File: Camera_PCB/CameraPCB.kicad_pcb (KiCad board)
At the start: 6 copper layers, 65.6 x 55 mm, 173 parts, among them J1 MIPI-CSI2, J2 USB_A, J3 SDA, J4 UART_0, J5 UART_2, J6 USB_C_Receptacle_PowerOnly_6P, SW1 PWR, SW2 RST, U1 AXP203, U2 V3s-eLQFP128, U3 TPS63020, U4 TPS63020, Y2 32.768kHz XTAL, Y4 24MHz XTAL

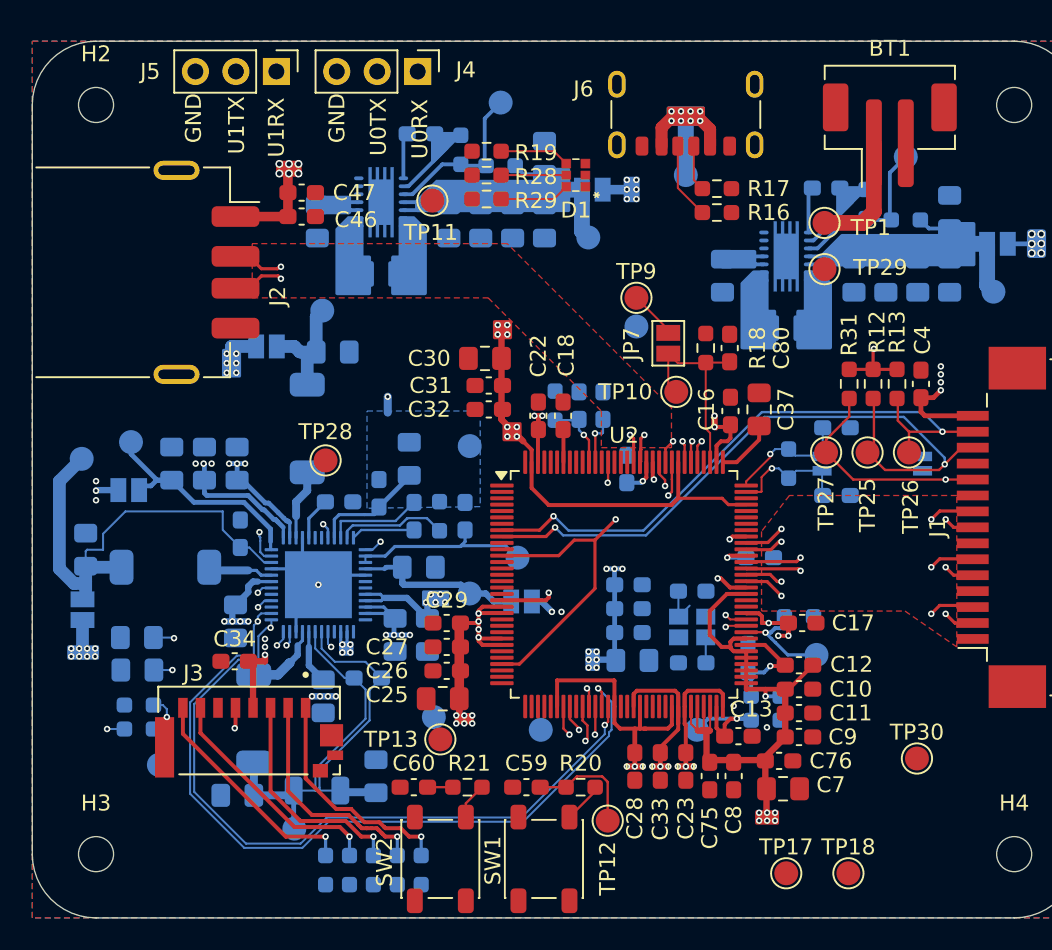
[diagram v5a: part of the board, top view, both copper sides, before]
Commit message: Only unconnected grounds in schematic. Still need to thoroughly clean up.
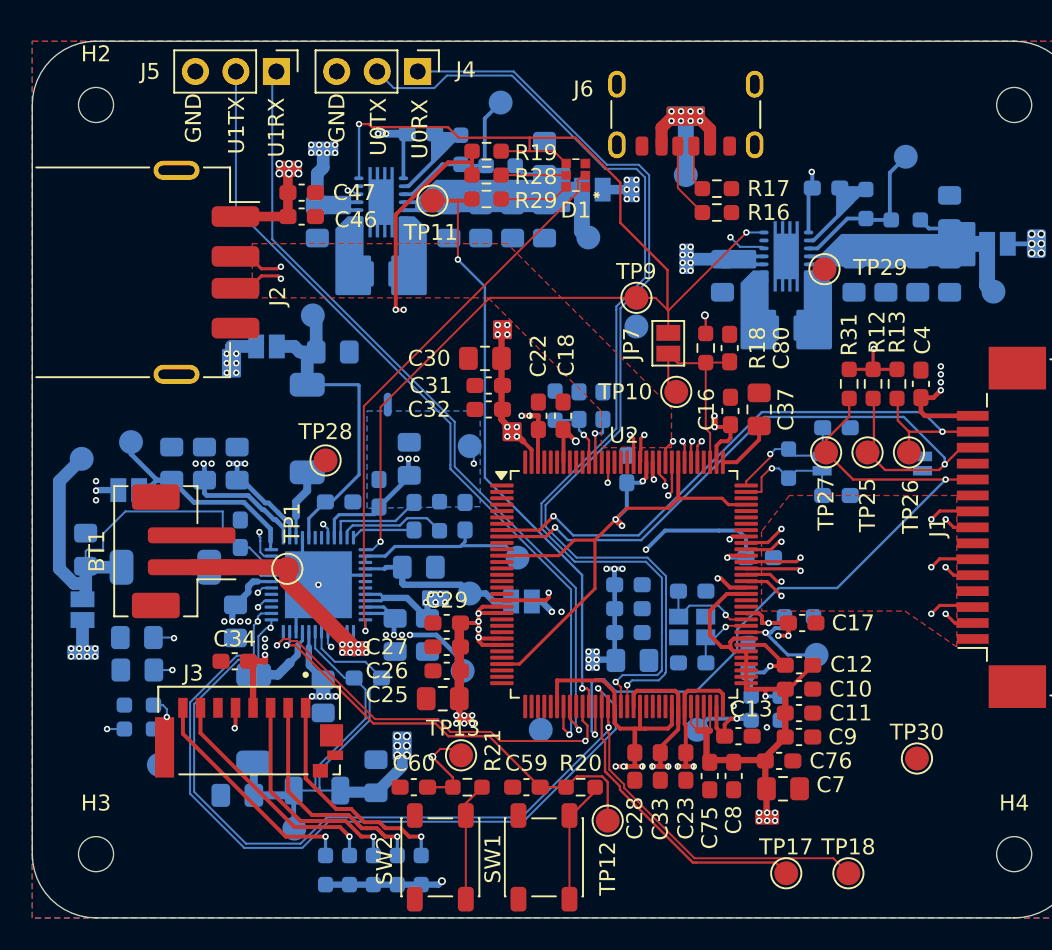
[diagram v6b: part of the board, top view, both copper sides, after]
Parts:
- moved BT1 51.4 mm to (124.5, 96.0), turned to 90 degrees
- moved TP1 40.1 mm to (131.0, 97.1), turned to 90 degrees
- moved TP2 3.42 mm to (142.0, 103.5)
- moved TP13 1.64 mm to (141.9, 108.8)
- moved TP4 0.66 mm to (132.6, 81.2)
- moved SW1 0.10 mm to (147.1, 115.2)
- moved SW2 0.10 mm to (140.6, 115.2)
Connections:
- D1 pad 4: Net-(D1-BA) -> PGOOD
- R19 pad 1: PGOOD -> HPVCC
- R19 pad 2: Net-(D1-BA) -> PGOOD
- R28 pad 1: VIPS -> HPVCC
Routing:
- net VIPS: track 37.4 -> 165.4 mm, vias 16 -> 22
- net VBAT: track 34.2 -> 136.6 mm, vias 4 -> 30
- net PGOOD: track 4.19 -> 76.0 mm, vias 1 -> 3
- net PWREN: track 0.97 -> 69.2 mm, vias 1 -> 4
- net UART0_TX: track 0.00 -> 64.4 mm, vias 0 -> 1
- net UART0_RX: track 0.00 -> 61.0 mm, vias 0 -> 1
- net HPVCC: track 227.5 -> 282.6 mm, vias 31 -> 36
- net UART2_TX: track 1.92 -> 52.3 mm
- net UART2_RX: track 1.71 -> 51.1 mm
- net STATUS_LED: track 1.19 -> 37.8 mm, vias 1 -> 2
- net CHGLED: track 0.00 -> 35.2 mm, vias 0 -> 1
- net CAM_EN0: track 15.8 -> 48.0 mm
- net IRQ: track 3.36 -> 25.5 mm
- net Net-(U1-N_OE): track 2.60 -> 24.2 mm, vias 1 -> 2
- net TWI0_SDA: track 45.5 -> 66.0 mm
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
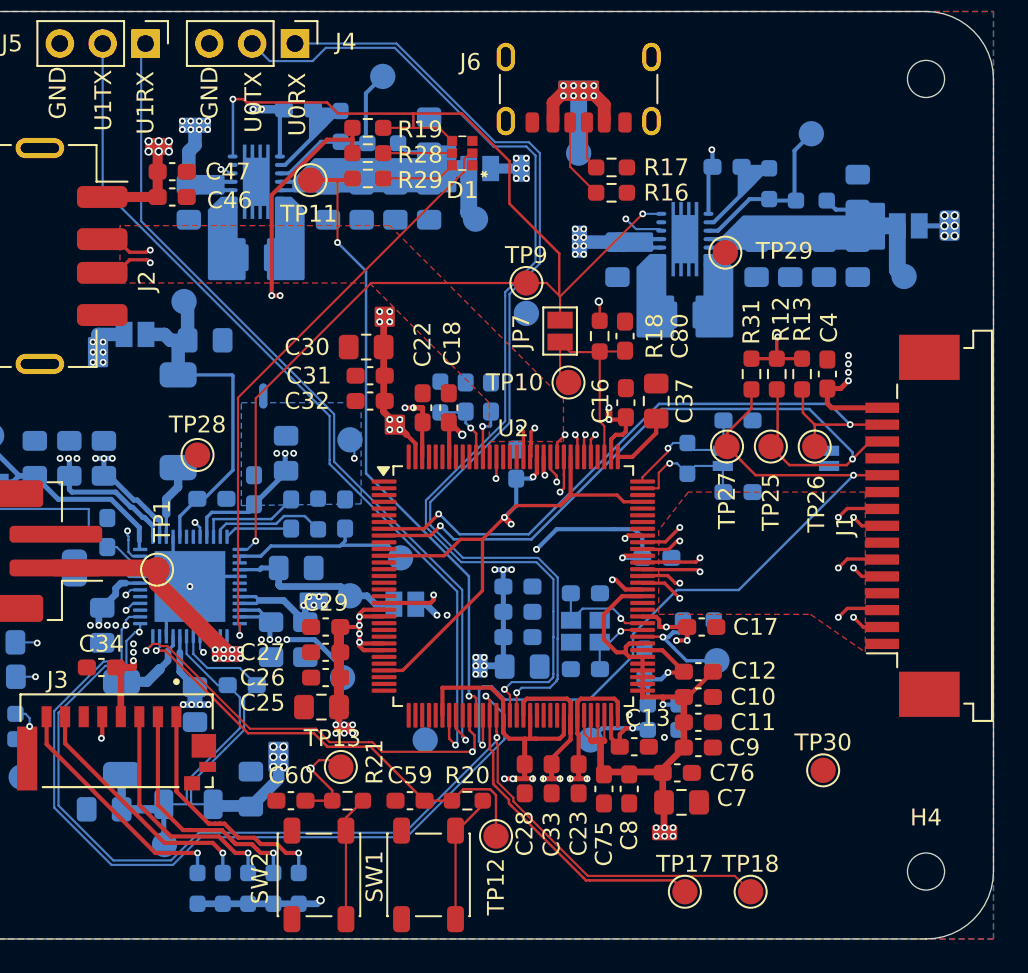
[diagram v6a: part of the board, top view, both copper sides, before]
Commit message: replaced all power traces with zones
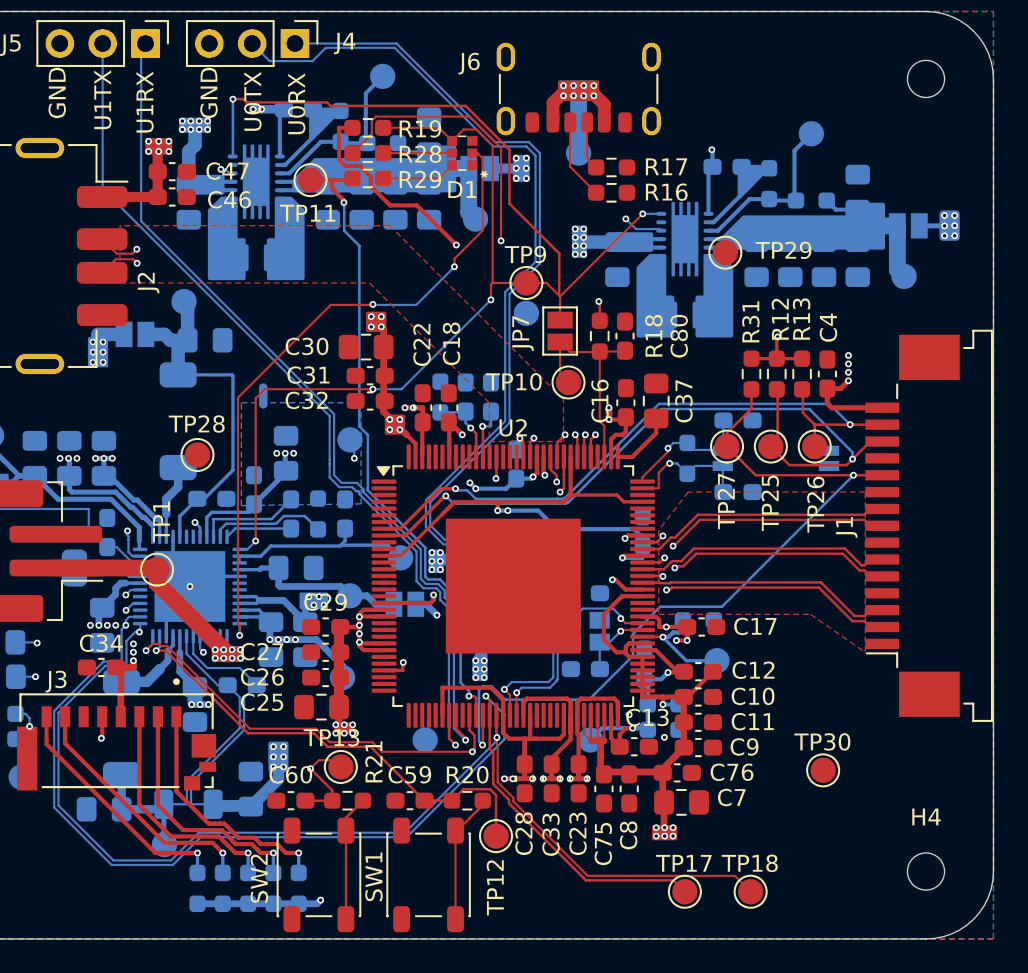
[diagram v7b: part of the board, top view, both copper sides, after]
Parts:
- moved C19 2.06 mm to (151.3, 101.2)
- moved C20 2.06 mm to (151.1, 98.0)
- moved C21 2.06 mm to (151.1, 99.5)
- moved C24 2.06 mm to (151.1, 96.5)
- moved C15 1.81 mm to (159.8, 94.8), turned to -90 degrees
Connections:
- R28 pad 1: HPVCC -> VBUS
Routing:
- net HPVCC: track 282.6 -> 106.3 mm, vias 36 -> 37
- net VIPS: track 165.4 -> 44.6 mm, vias 22 -> 21
- net VDD-CPU: track 167.5 -> 65.5 mm, vias 38 -> 41
- net VBAT: track 136.6 -> 49.1 mm
- net AVCC: track 82.1 -> 7.31 mm
- net VCC-DRAM: track 112.4 -> 41.4 mm
- net +5V: track 59.4 -> 7.92 mm
- net VCC-RTC: track 41.8 -> 7.53 mm, vias 5 -> 4
- net VBUS: track 51.4 -> 31.6 mm
- net PGOOD: track 76.0 -> 87.3 mm, vias 3 -> 5
- net CHGLED: track 35.2 -> 38.9 mm, vias 1 -> 3
- net USB_P: track 32.1 -> 33.3 mm
- net SDC0_D1: track 50.1 -> 51.4 mm
- net SDC0_CLK: track 47.4 -> 48.7 mm
- net UART2_RX: track 51.1 -> 52.0 mm
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- added copper zone on In2.Cu, net +5V
- added copper zone on In3.Cu, net AVCC
- added copper zone on In3.Cu, net HPVCC
- added copper zone on In2.Cu, net VBAT
- added copper zone on In3.Cu, net VBAT
- added copper zone on In3.Cu, net VBUS
- added copper zone on In2.Cu, net VCC-DRAM
- added copper zone on In3.Cu, net VCC-RTC
- added copper zone on In2.Cu, net VDD-CPU
- added copper zone on In2.Cu, net VIPS

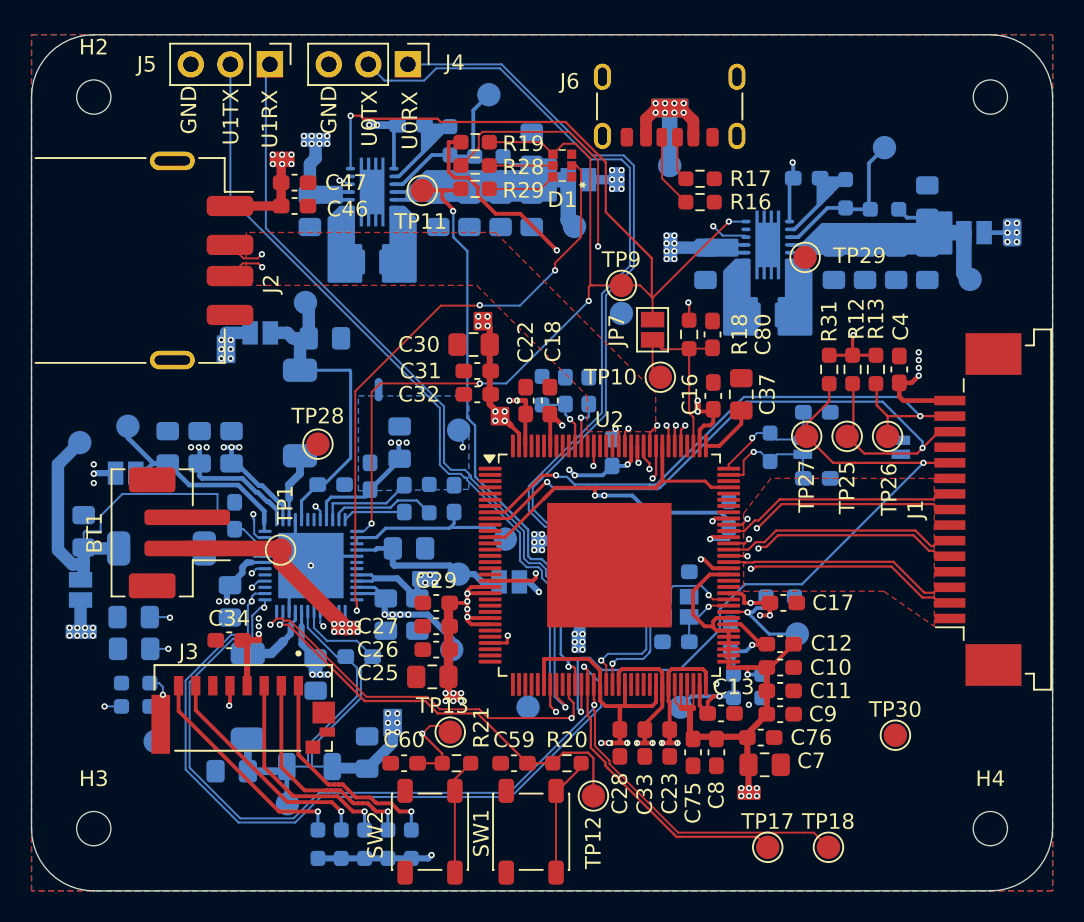
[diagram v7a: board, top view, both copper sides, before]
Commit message: PCB has no missing connections, (some missing grounds)
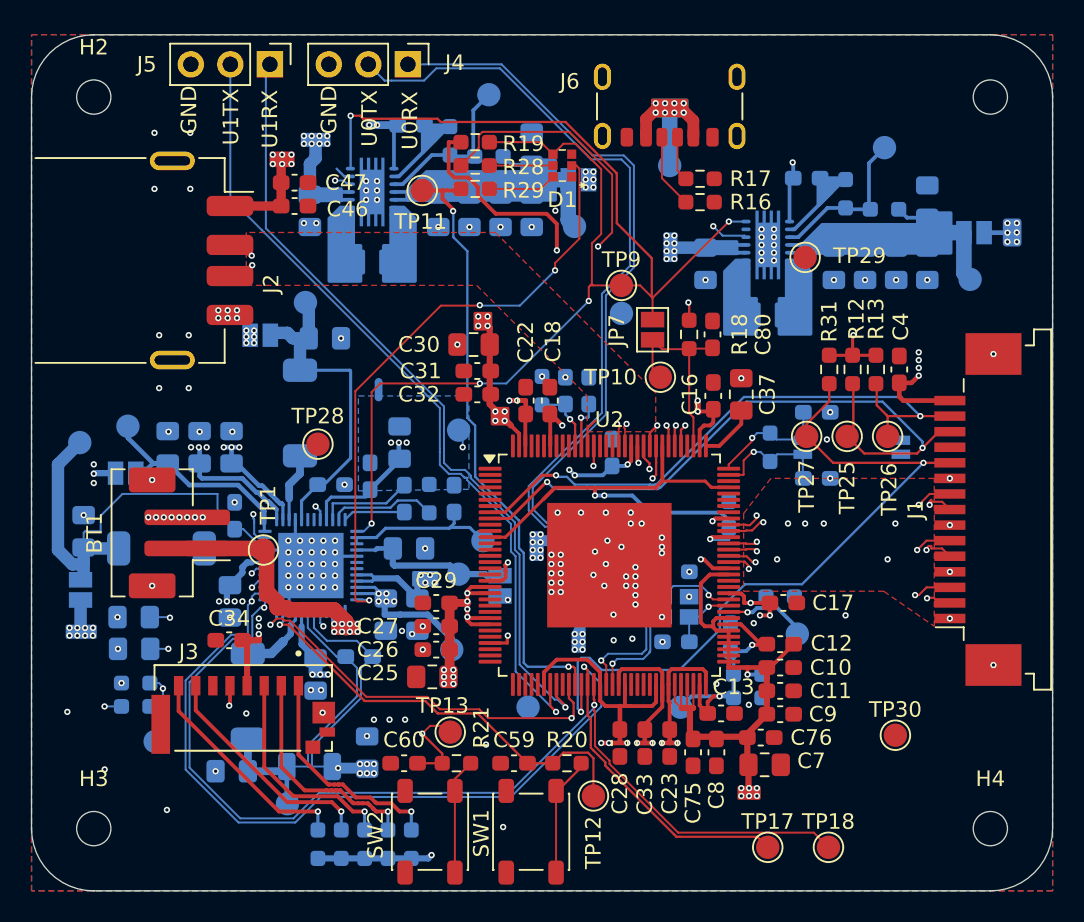
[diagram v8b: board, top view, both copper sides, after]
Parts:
- moved TP6 1.45 mm to (144.0, 96.5)
- moved TP1 1.10 mm to (129.9, 97.1)
- moved JP1 0.64 mm to (145.1, 99.4), turned to -90 degrees
- moved JP4 0.15 mm to (129.7, 83.3)
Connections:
- BT1 pad MP: (no net) -> GND
- U2 pad 129: (no net) -> GND
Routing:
- net VDD-CPU: track 65.5 -> 62.4 mm, vias 41 -> 43
- net VCC-DRAM: track 41.4 -> 38.4 mm
- net GND: track 15.5 -> 18.4 mm, vias 3 -> 169
- net VBAT: track 49.1 -> 47.0 mm, vias 30 -> 31
- net USB_P: track 33.3 -> 31.6 mm
- net USB_N: track 33.9 -> 32.1 mm
- net VCC-RTC: track 7.53 -> 6.00 mm
- net VINT: track 11.6 -> 10.2 mm
- net STATUS_LED: track 38.4 -> 39.5 mm
- net HPVCC: track 106.3 -> 105.5 mm
- net VBUS: track 31.6 -> 32.3 mm
- net PGOOD: track 87.3 -> 87.9 mm
- net SZQ: track 6.88 -> 6.33 mm
- net SDC0_D2: track 47.9 -> 48.4 mm
- net SDC0_D3: track 48.9 -> 49.4 mm
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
